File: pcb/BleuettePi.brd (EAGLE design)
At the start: 85 x 56 mm, 106 parts, among them IC1 PIC18F452, IC2 DS1307, IC3 MAX4173FESA+, IC5 MCP23017SS, IC6 LM386M-1, IC7 GY-27, Q1 10Mhz, Q6 32.768KHz

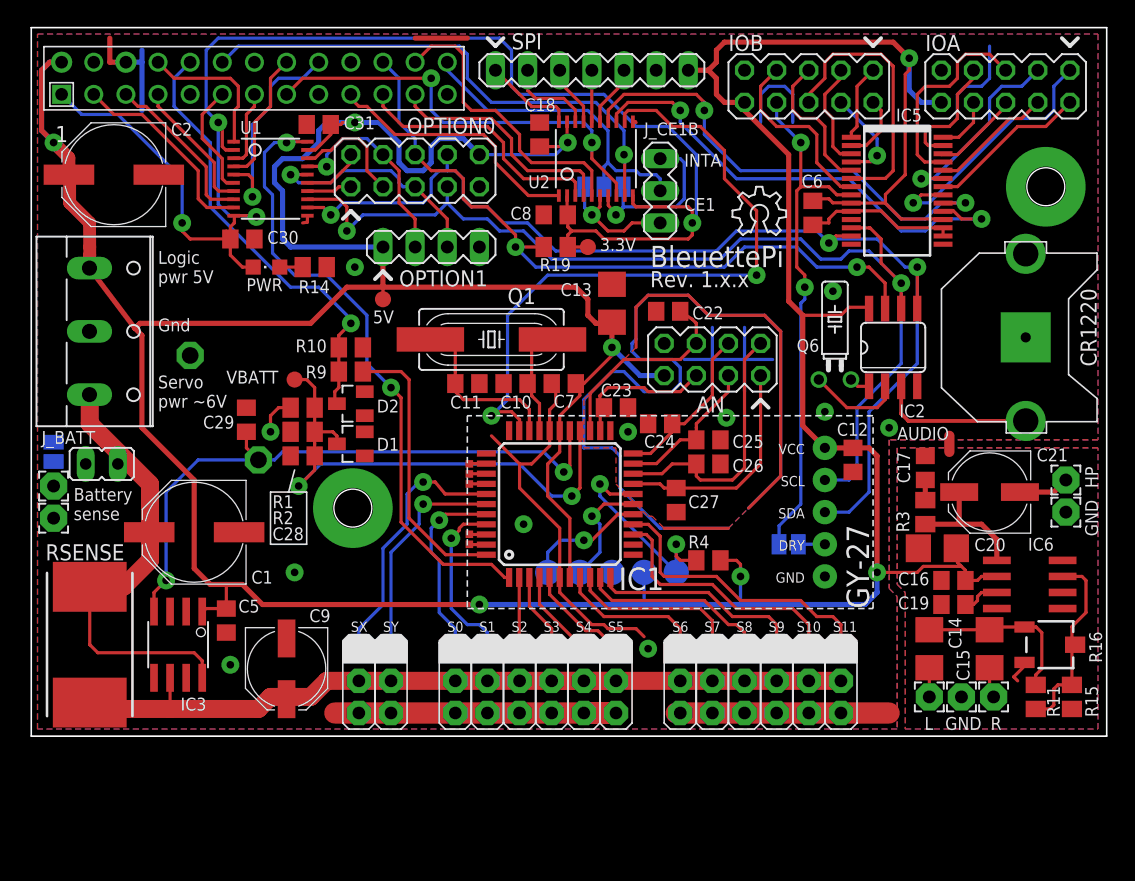
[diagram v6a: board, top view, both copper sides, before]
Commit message: I2C linked to Pic + Misc
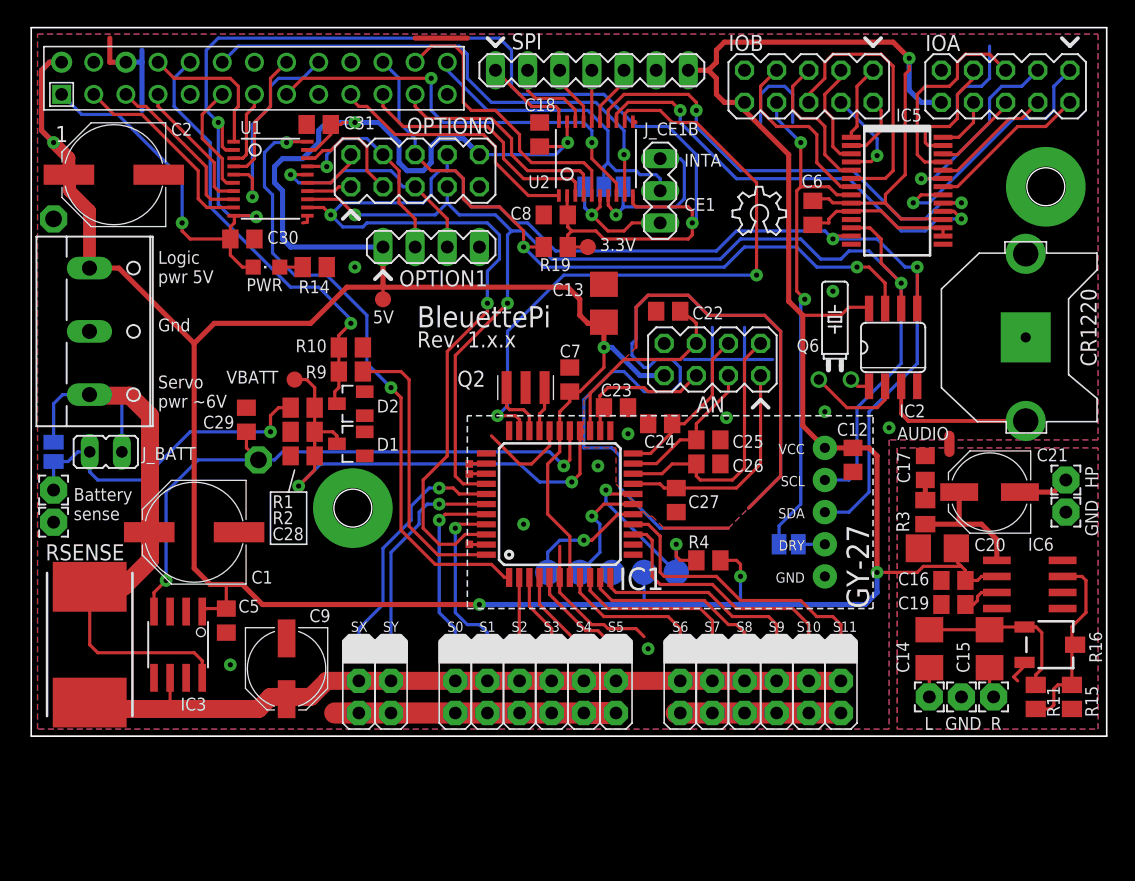
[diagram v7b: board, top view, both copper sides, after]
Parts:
- removed C10, C11: 22pf, rcl:C0805
- removed Q1: 10Mhz, crystal:HC49UP@1
- removed RC3, RC4: TPSQTP06SQ, testpad:TP06SQ
- added Q2: 10Mhz, murata-filter:CSTCR6M
- R1: value 3.3k -> 15k
- moved TP1 15.3 mm to (1.91, 41.0)
- moved J_BATT1 1.00 mm to (6.03, 22.5), turned to 90 degrees
- moved C13 0.63 mm to (45.4, 34.3)
- moved C7 0.57 mm to (42.7, 28.3), turned to 90 degrees
- moved BATT1 0.32 mm to (1.91, 17.0)
- moved BATT 0.32 mm to (1.91, 19.5)
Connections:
- removed net GPB6: IC5.7, IOB.7
- removed net N$25: C11.2, IC1.31, Q1.1
- removed net N$27: C10.2, IC1.30, Q1.2
- removed net RC3: IC1.37, RC3.TP
- removed net RC4: IC1.42, RC4.TP
- new net N$1: IC1.31, Q2.3
- new net N$2: IC1.30, Q2.1
- net SCL: now also IC1.37
- net SDA: now also IC1.42
- net UC_RESET: now also IC5.7, IOB.7
- net VSS: now also Q2.2; no longer C10.1, C11.1
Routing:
- net SDA: track 86.4 -> 131.4 mm, vias 3 -> 4
- net VDD: track 3.12 -> 26.3 mm
- net SCL: track 83.8 -> 105.5 mm, vias 2 -> 3
- net VSS: track 117.7 -> 101.4 mm, vias 10 -> 8
- net +7V: track 36.9 -> 51.7 mm
- net GPB6: track 14.7 -> 0.00 mm
- net N$25: track 14.2 -> 0.00 mm
- net N$27: track 13.6 -> 0.00 mm
- net UC_RESET: track 17.3 -> 30.7 mm
- net N$1: track 0.00 -> 4.80 mm
- net N$2: track 0.00 -> 3.57 mm
- net INTB: track 38.3 -> 35.1 mm
- net INTD: track 53.8 -> 52.1 mm
- net AN6: track 41.6 -> 40.0 mm
- net RC4: track 1.35 -> 0.00 mm
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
